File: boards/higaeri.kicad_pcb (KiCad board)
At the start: 2 copper layers, 98.8 x 94 mm, 80 parts, among them J1 5051104096, J10 Conn_01x04, J11 RE12A, J12 RS485_airdata, J13 Conn_01x03 speaker, J2 Micro_SD_Card, J3 URM37, J4 Conn_01x03 servo, J5 RS485_TFT, J6 Conn_01x03 encoder_direct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

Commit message: 増幅回路追加
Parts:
- added D3: LED, LED_SMD:LED_0603_1608Metric_Pad1.05x0.95mm_HandSolder, F.Cu at (111.1, 74.6)
- added J14: RE12A, Connector_JST:JST_XH_S4B-XH-SM4-TB_1x04-1MP_P2.50mm_Horizontal, F.Cu at (93.3, 92.4)
- added J15: encoder_direct, Connector_JST:JST_PH_S3B-PH-K_1x03_P2.00mm_Horizontal, F.Cu at (106.5, 91.5)
- added Q1: NPN, Package_TO_SOT_SMD:SOT-23, F.Cu at (111.3, 71.0)
- added Q2: NPN, Package_TO_SOT_SMD:SOT-23, F.Cu at (127.5, 73.5)
- added R15: 100, Resistor_SMD:R_0603_1608Metric_Pad0.98x0.95mm_HandSolder, F.Cu at (106.7, 63.5)
- added R16: 2k2, Resistor_SMD:R_0603_1608Metric_Pad0.98x0.95mm_HandSolder, F.Cu at (106.7, 66.0)
- added R19: 10k, Resistor_SMD:R_0603_1608Metric_Pad0.98x0.95mm_HandSolder, F.Cu at (106.7, 68.5)
- added R21: 10k, Resistor_SMD:R_0603_1608Metric_Pad0.98x0.95mm_HandSolder, F.Cu at (106.7, 71.0)
- added R37: 10k, Resistor_SMD:R_0603_1608Metric_Pad0.98x0.95mm_HandSolder, F.Cu at (106.7, 73.5)
- added R38: 10k, Resistor_SMD:R_0603_1608Metric_Pad0.98x0.95mm_HandSolder, F.Cu at (106.7, 76.0)
- added R39: 150, Resistor_SMD:R_0603_1608Metric_Pad0.98x0.95mm_HandSolder, F.Cu at (106.7, 78.6)
- added R40: 10k, Resistor_SMD:R_0603_1608Metric_Pad0.98x0.95mm_HandSolder, F.Cu at (106.7, 81.1)
- added R41: 10k, Resistor_SMD:R_0603_1608Metric_Pad0.98x0.95mm_HandSolder, F.Cu at (121.5, 63.5)
- added R42: 10k, Resistor_SMD:R_0603_1608Metric_Pad0.98x0.95mm_HandSolder, F.Cu at (121.5, 66.0)
- added R43: 2k2, Resistor_SMD:R_0603_1608Metric_Pad0.98x0.95mm_HandSolder, F.Cu at (121.5, 68.5)
- added R44: 10k, Resistor_SMD:R_0603_1608Metric_Pad0.98x0.95mm_HandSolder, F.Cu at (121.5, 71.0)
- added R45: 10k, Resistor_SMD:R_0603_1608Metric_Pad0.98x0.95mm_HandSolder, F.Cu at (121.5, 73.5)
- added R46: 10k, Resistor_SMD:R_0603_1608Metric_Pad0.98x0.95mm_HandSolder, F.Cu at (121.5, 76.0)
- added U10: LM397, Package_SO:SOP-8_3.9x4.9mm_P1.27mm, F.Cu at (127.9, 65.6)
- added U3: MOUDLE-SEEEDUINO-XIAO-ESP32C3_airdata, footprints:XIAO-ESP32C3-SMD, F.Cu at (94.5, 74.8)
- added U7: TJ393, Package_SO:SOP-8_3.9x4.9mm_P1.27mm, F.Cu at (114.5, 57.0)
- AS5603: footprint Connector_PinHeader_2.54mm:PinHeader_1x06_P2.54mm_Horizontal -> Connector_PinHeader_2.54mm:PinHeader_1x06_P2.54mm_Vertical
- C2: footprint Capacitor_SMD:C_0603_1608Metric_Pad1.08x0.95mm_HandSolder -> Capacitor_SMD:C_1210_3225Metric_Pad1.33x2.70mm_HandSolder
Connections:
- J11 pad 2: Net-(J11-Pin_2) -> /1. airdata/encoder_collector

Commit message: DRCエラー解消
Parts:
- removed Q3: NPN, Package_TO_SOT_SMD:SOT-23
- removed R25: 20k, Resistor_SMD:R_0603_1608Metric_Pad0.98x0.95mm_HandSolder
- removed R27: 3k, Resistor_SMD:R_0603_1608Metric_Pad0.98x0.95mm_HandSolder
- removed R29: 100k, Resistor_SMD:R_0603_1608Metric_Pad0.98x0.95mm_HandSolder
- removed R30: 10k, Resistor_SMD:R_0603_1608Metric_Pad0.98x0.95mm_HandSolder
- removed the REF** at (148.0, 118.0)
- added Batt5: Conn_01x02, Connector_JST:JST_PH_S2B-PH-SM4-TB_1x02-1MP_P2.00mm_Horizontal, B.Cu at (246.5, 138.9)
- J14, Q1, R19, R21, R37, R38, R39, R40, R43: moved to B.Cu
- J4: value Conn_01x03 servo -> servo
- J6: value Conn_01x03 encoder_direct -> encoder_direct
- R26: value 330 -> 150; moved to B.Cu
- U1, U11, U3, U5, U9: footprint footprints:XIAO-ESP32C3-SMD -> footprints:XIAO-ESP32C3-SMD_battery_handsolder
- U10: value LM397 -> TJ393
- moved R15 165.5 mm to (244.6, 154.9)
- moved D3 159.3 mm to (248.6, 154.9), turned to 180 degrees
- moved R16 157.0 mm to (244.6, 140.9), turned to -90 degrees
- moved U7 156.5 mm to (248.1, 138.4), turned to 90 degrees
- moved U3 155.4 mm to (233.1, 144.9), turned to 180 degrees
- moved J15 150.2 mm to (244.7, 150.4), turned to 90 degrees
- moved R37 146.6 mm to (236.6, 141.3), turned to 90 degrees
- moved R19 146.3 mm to (233.6, 141.3), turned to 90 degrees
- moved R40 145.5 mm to (239.1, 141.3), turned to 90 degrees
- moved R38 143.9 mm to (236.6, 137.8), turned to 90 degrees
- moved R39 143.9 mm to (233.5, 146.4), turned to 180 degrees
- moved R21 143.4 mm to (233.6, 137.8), turned to 90 degrees
- moved J14 142.0 mm to (225.6, 143.9), turned to 90 degrees
- moved Q1 135.9 mm to (230.1, 136.9), turned to 90 degrees
- moved R42 120.4 mm to (235.0, 106.0), turned to 90 degrees
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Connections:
- J15 pad 1: +3.3V-3 -> +3.3V-4
- J15 pad 2: GND-3 -> GND-4
- U7 pad 4: GND-3 -> GND-4
- U7 pad 8: +3.3V-3 -> +3.3V-4
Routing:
- net +3.3V-4: track 0.00 -> 65.9 mm, vias 0 -> 1
- net +BATT-2: track 120.4 -> 69.6 mm, vias 4 -> 1
- net /RE12A_amplifier/encoder_out: track 0.00 -> 34.7 mm, vias 0 -> 2
- net /2.logger/DE/RE: track 40.1 -> 5.55 mm, vias 3 -> 1
- net GND-4: track 0.00 -> 29.5 mm, vias 0 -> 14
- net /RE12A_amplifier/input: track 0.00 -> 27.1 mm, vias 0 -> 1
- net +3.3V-1: track 84.5 -> 110.6 mm, vias 3 -> 4
- net GND-1: track 179.2 -> 155.3 mm, vias 31 -> 32
- net /2.logger/SCL: track 82.6 -> 106.4 mm, vias 1 -> 2
- net /2.logger/SCLK: track 22.5 -> 45.8 mm, vias 2 -> 0
- net /2.logger/V_check-2: track 5.73 -> 27.5 mm, vias 2 -> 1
- net /1. airdata/input: track 0.00 -> 20.2 mm, vias 0 -> 2
- net /2.logger/SDA: track 71.8 -> 91.1 mm, vias 2 -> 1
- net Net-(U5-GPIO3_A1_D1): track 60.6 -> 41.9 mm
- net Net-(U2-DI): track 5.55 -> 23.1 mm
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- added copper zone on B.Cu, net GND-4
- added copper zone on F.Cu, net GND-4
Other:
- board size 98.8 x 94 mm -> 108.6 x 127.9 mm
- board text removed: "RE12E"

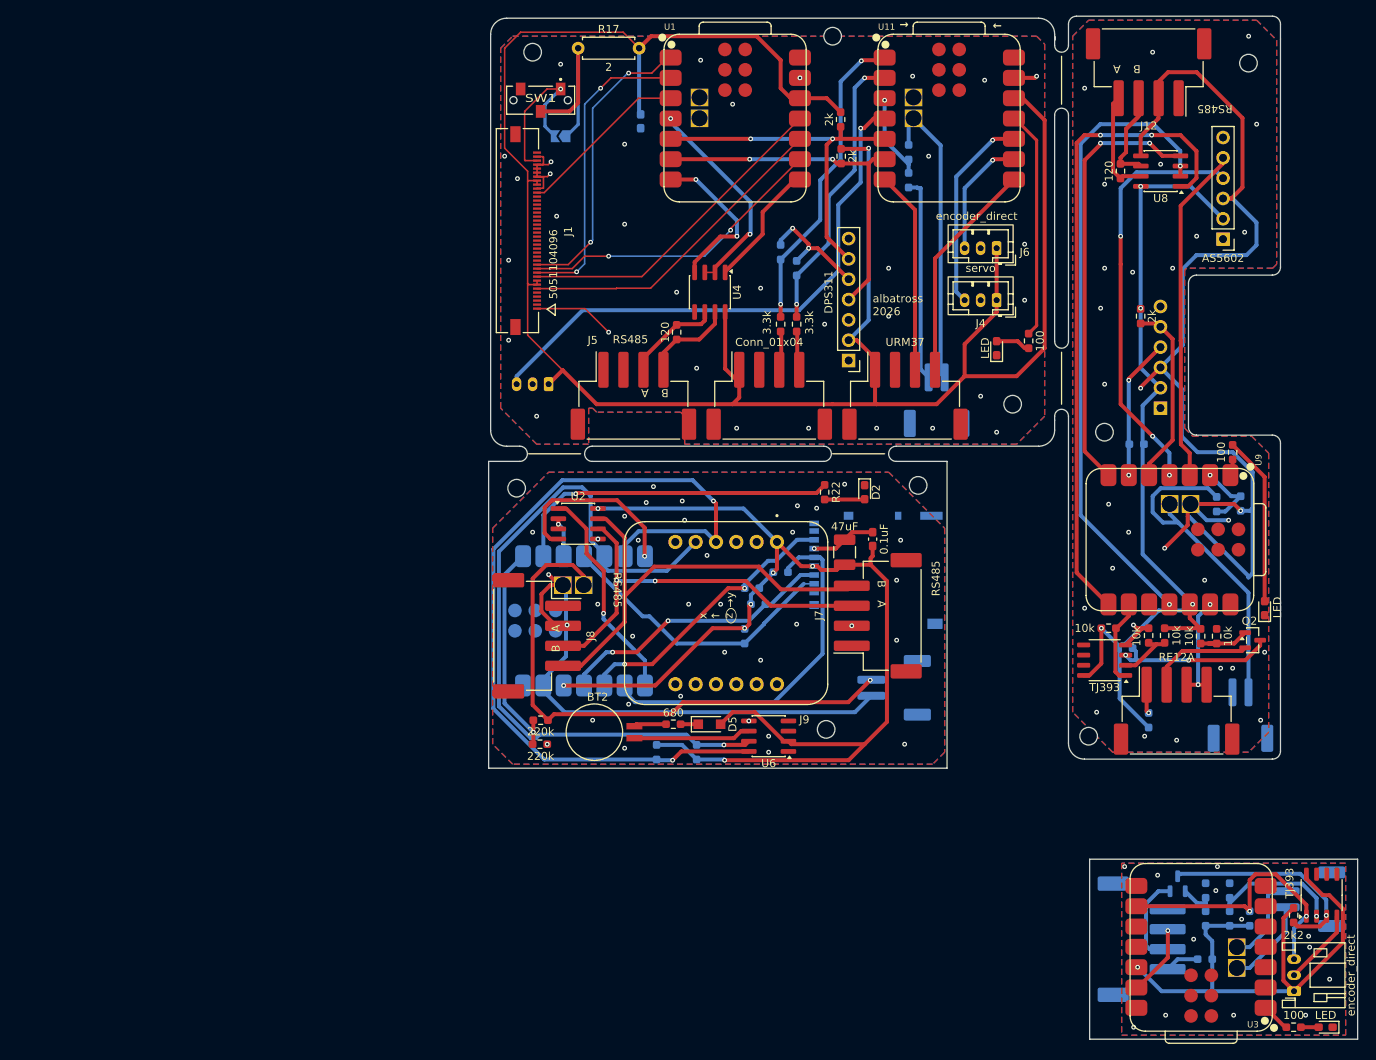
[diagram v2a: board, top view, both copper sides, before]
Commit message: シルクスクリーン修正
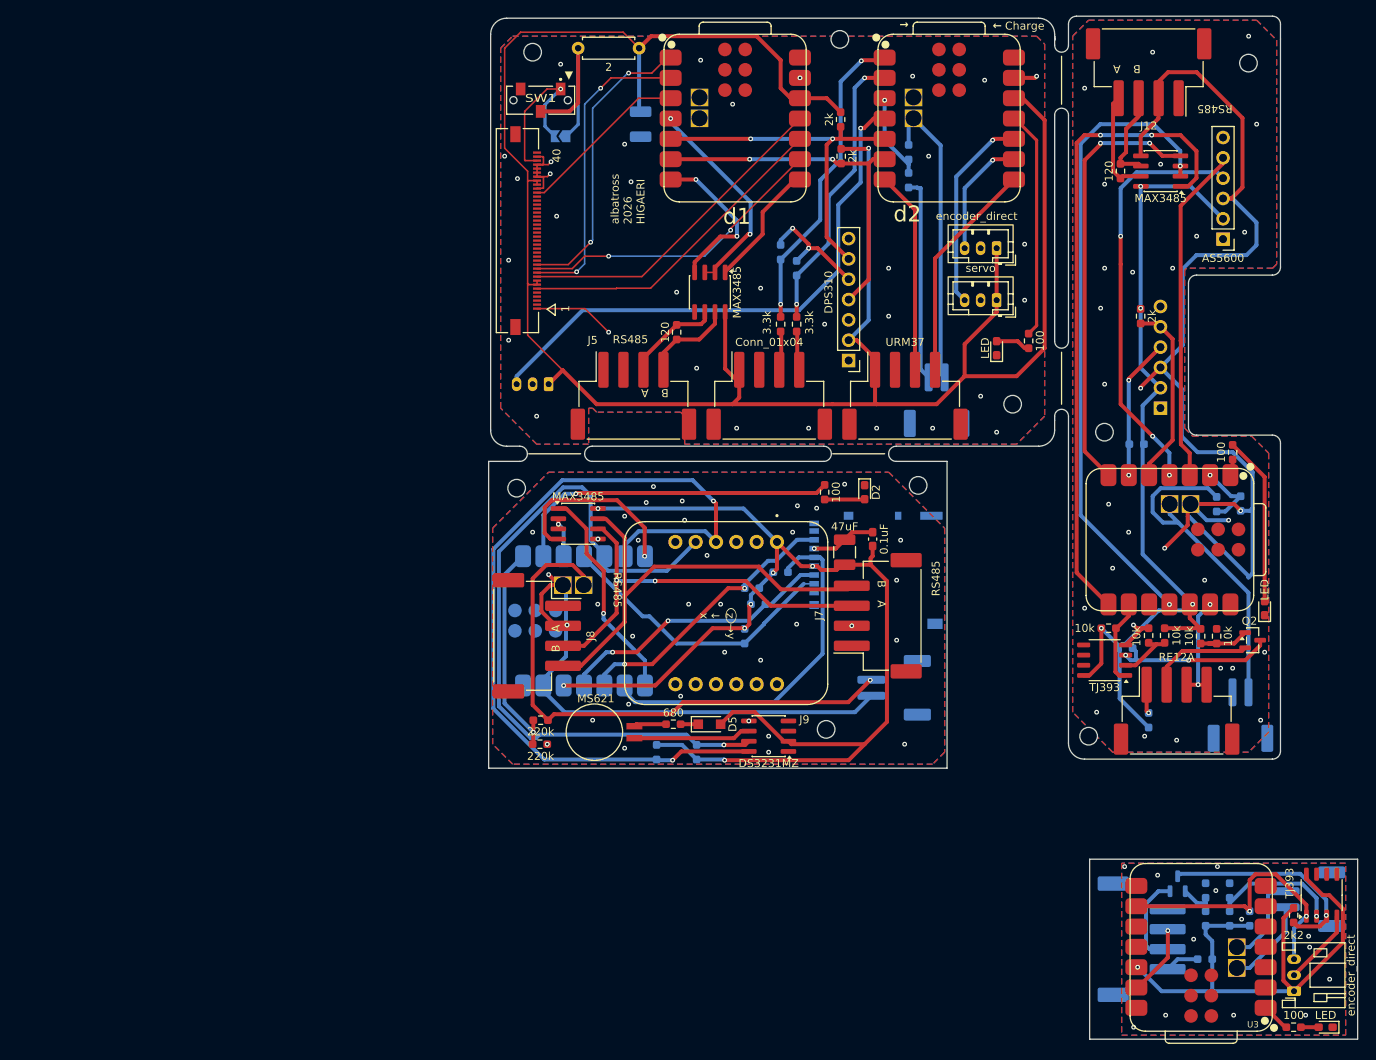
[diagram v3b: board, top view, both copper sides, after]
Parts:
- C3: footprint Capacitor_SMD:C_0603_1608Metric_Pad1.08x0.95mm_HandSolder -> Capacitor_SMD:C_1210_3225Metric_Pad1.33x2.70mm_HandSolder
- moved REF** 0.98 mm to (187.9, 31.4)
- moved C3 0.36 mm to (163.0, 42.0)
- renumbered AS5602 to AS5600, AS5603 to AS5600, DPS311 to DPS310
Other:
- board text added: "1"
- board text added: "40"
- board text added: "Charge"
- board text added: "albatross 2026 HIGAERI"
- board text added: "d1"
- board text added: "d2"
- board text added: "▼"
- board text removed: "albatross 2026"

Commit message: ファイル名変更
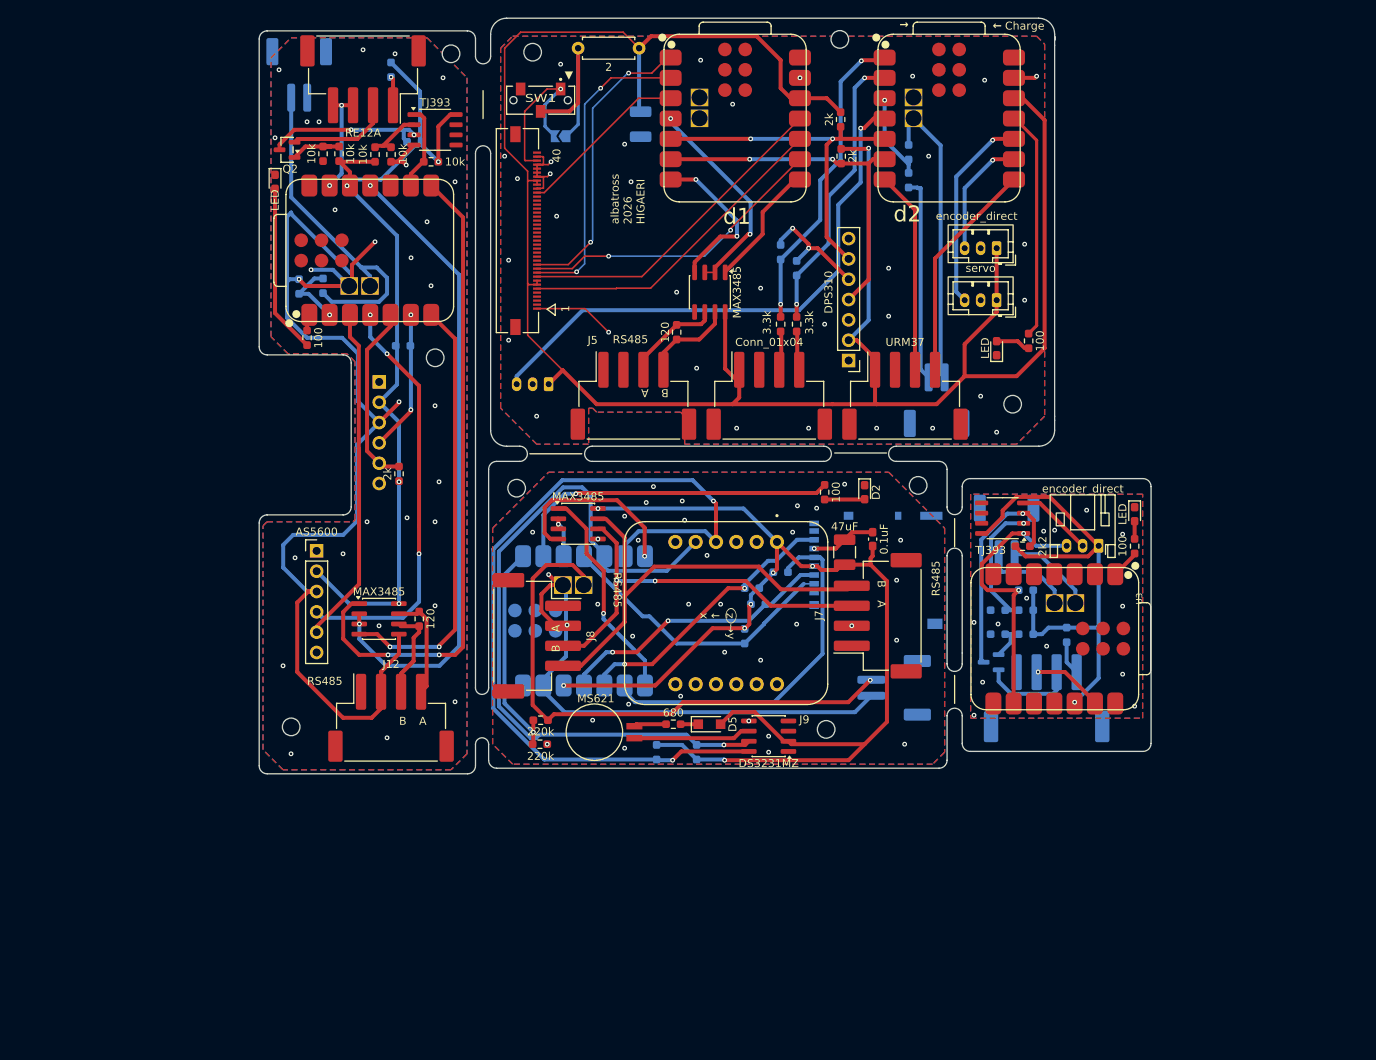
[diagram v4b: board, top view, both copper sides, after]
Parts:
- moved REF** 145.6 mm to (119.3, 117.3), turned to 0 degrees
- moved Batt4 142.3 mm to (120.3, 35.8), turned to 0 degrees
- moved Q2 135.4 mm to (118.8, 45.2), turned to 180 degrees
- moved D4 134.7 mm to (117.3, 49.2), turned to -90 degrees
- moved J11 128.7 mm to (128.3, 36.4), turned to 180 degrees
- moved R42 126.9 mm to (123.3, 45.7), turned to -90 degrees
- moved R26 124.8 mm to (131.8, 35.2), turned to -90 degrees
- moved J12 124.4 mm to (131.8, 116.2), turned to 0 degrees
- moved R41 123.4 mm to (125.3, 45.7), turned to 90 degrees
- moved R36 120.8 mm to (120.3, 62.3), turned to 90 degrees
- moved AS5600 119.8 mm to (122.5, 95.3), turned to 0 degrees
- moved REF** 116.7 mm to (139.3, 33.2), turned to 0 degrees
- moved R31 116.6 mm to (121.3, 68.7), turned to -90 degrees
- moved R44 115.6 mm to (129.8, 45.8), turned to 90 degrees
- moved R35 115.0 mm to (123.3, 62.2), turned to 90 degrees
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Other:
- board size 108.6 x 127.9 mm -> 111.5 x 94.4 mm

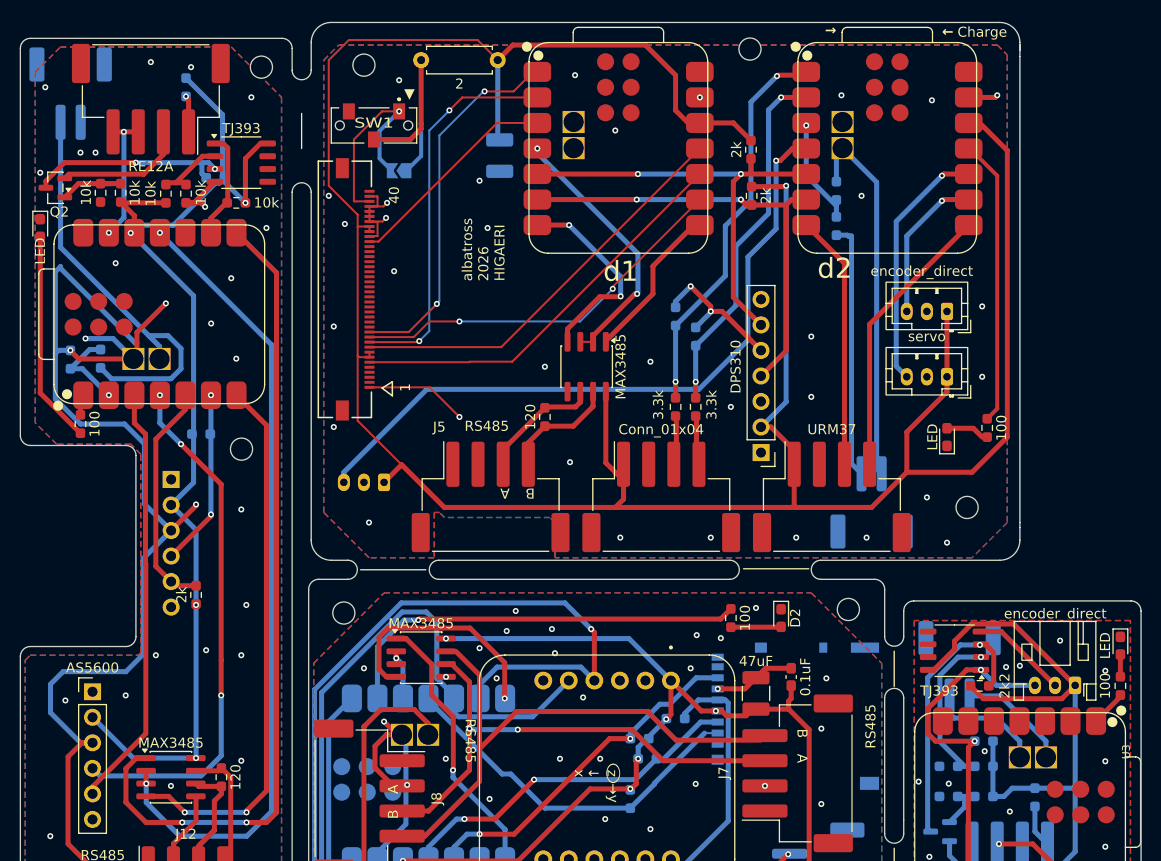
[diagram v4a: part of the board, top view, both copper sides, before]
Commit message: 動作確認をもとに統合版コード修正
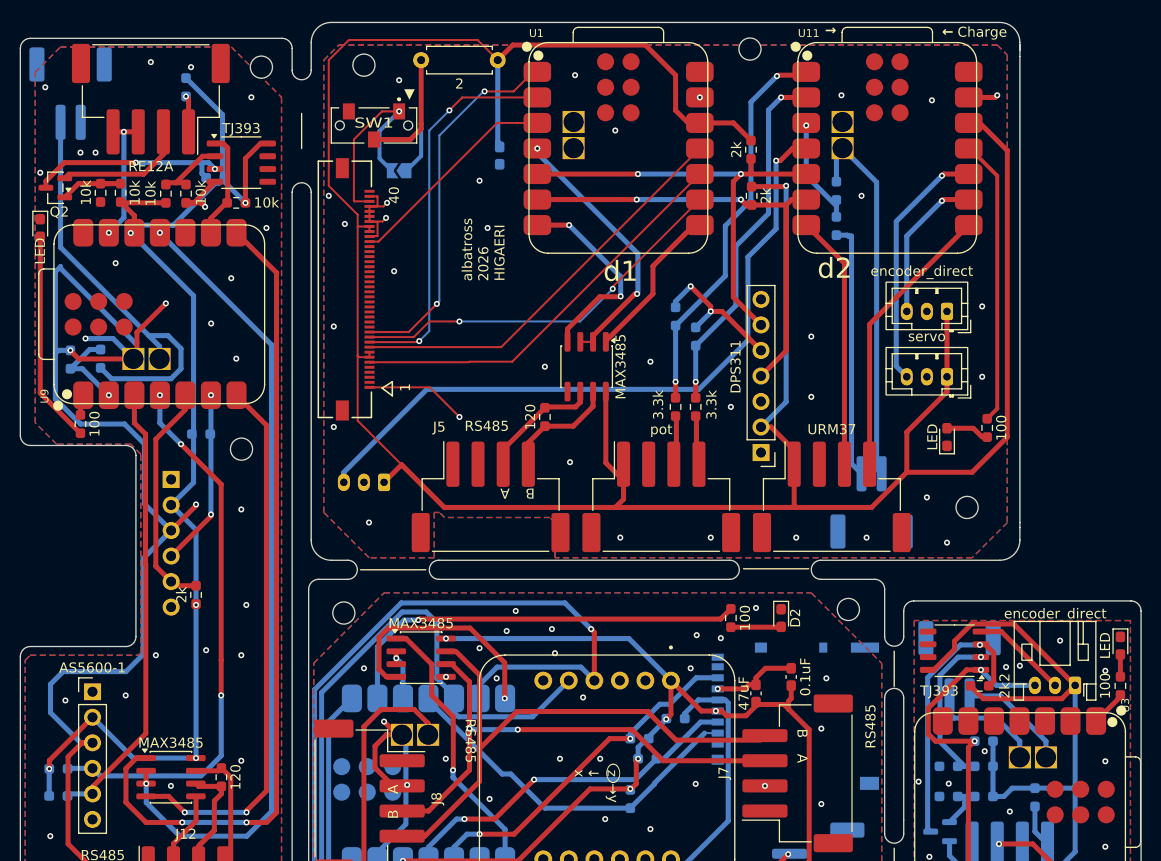
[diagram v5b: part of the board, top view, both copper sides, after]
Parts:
- added R25: 2k, Resistor_SMD:R_0603_1608Metric_Pad0.98x0.95mm_HandSolder, B.Cu at (119.1, 103.0)
- added R27: 2k, Resistor_SMD:R_0603_1608Metric_Pad0.98x0.95mm_HandSolder, B.Cu at (119.1, 105.7)
- C2, C3: footprint Capacitor_SMD:C_1210_3225Metric_Pad1.33x2.70mm_HandSolder -> Capacitor_SMD:C_0603_1608Metric_Pad1.08x0.95mm_HandSolder
- J10: value Conn_01x04 -> pot
- renumbered AS5600 to AS5600-1, AS5600 to AS5600-2, DPS310 to DPS311
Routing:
- net +3.3V-1: track 110.6 -> 120.2 mm, vias 4 -> 5
- net /1. airdata/SDA_soft: track 42.3 -> 44.9 mm
- net /1. airdata/SCL_soft: track 52.3 -> 54.8 mm
